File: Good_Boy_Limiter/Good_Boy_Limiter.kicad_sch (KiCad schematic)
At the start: 28 parts, among them Q2 AO3422, SW3 RESET1, SW4 BOOT1, U1 ESP32-S3-WROOM-1, U2 TC4427EOA_C636891, U3 LM2576HVR-12, U8 B3B-XH-A, U9 LM393DR2G

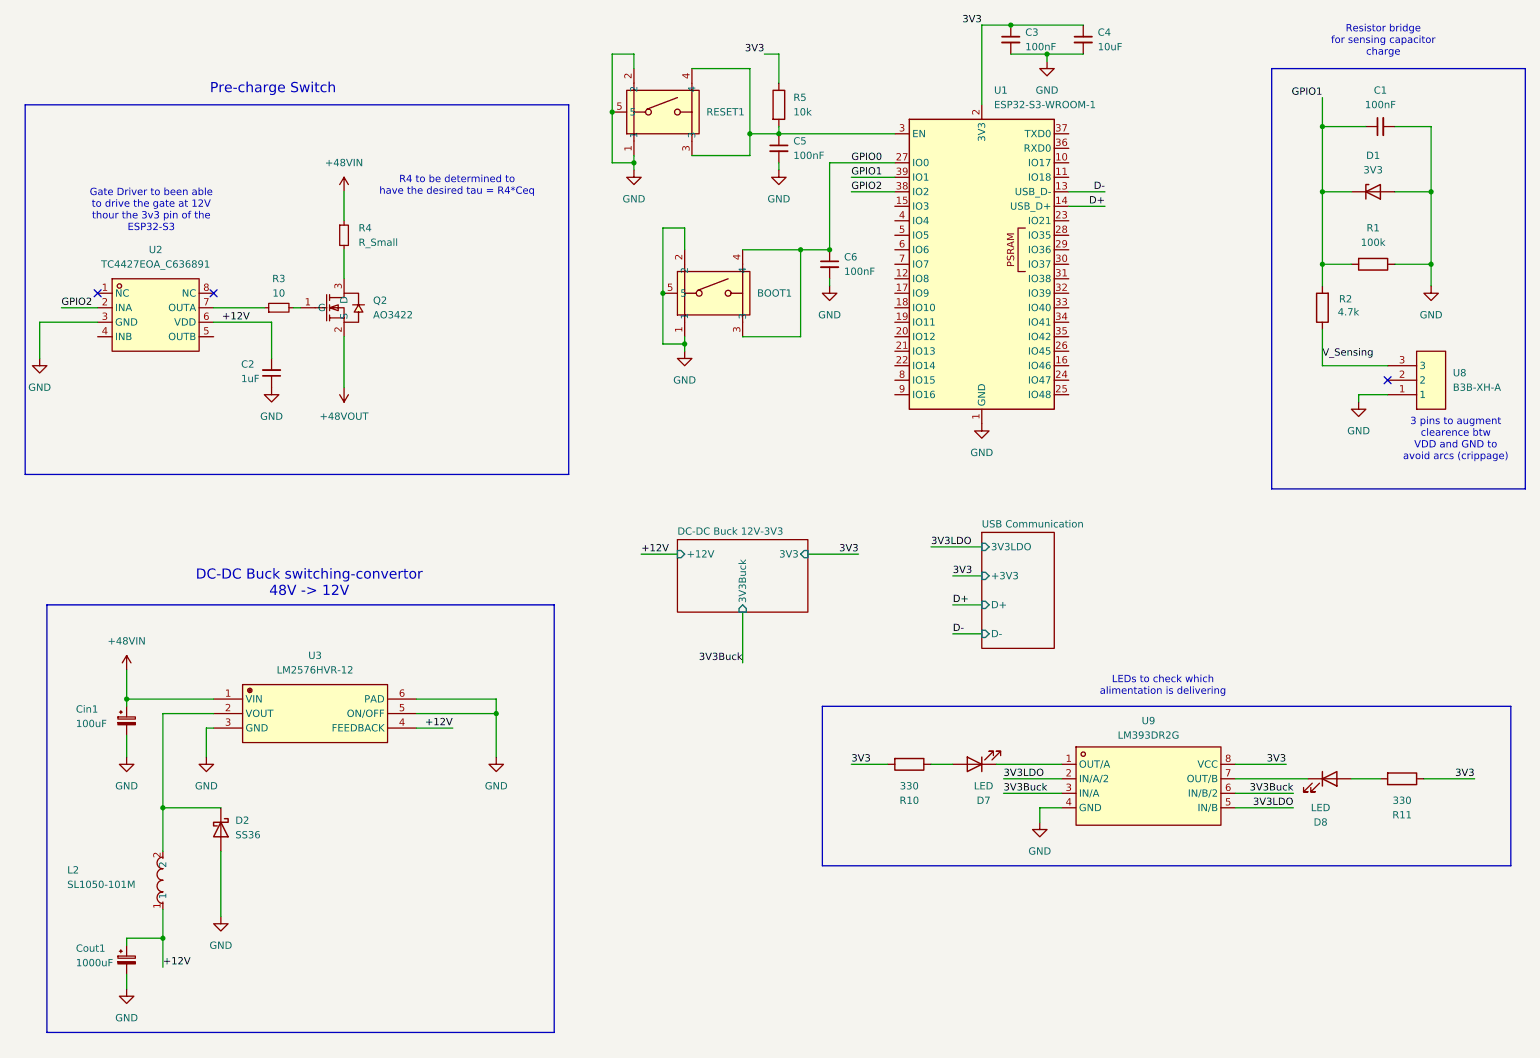
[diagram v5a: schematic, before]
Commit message: Added all footprints
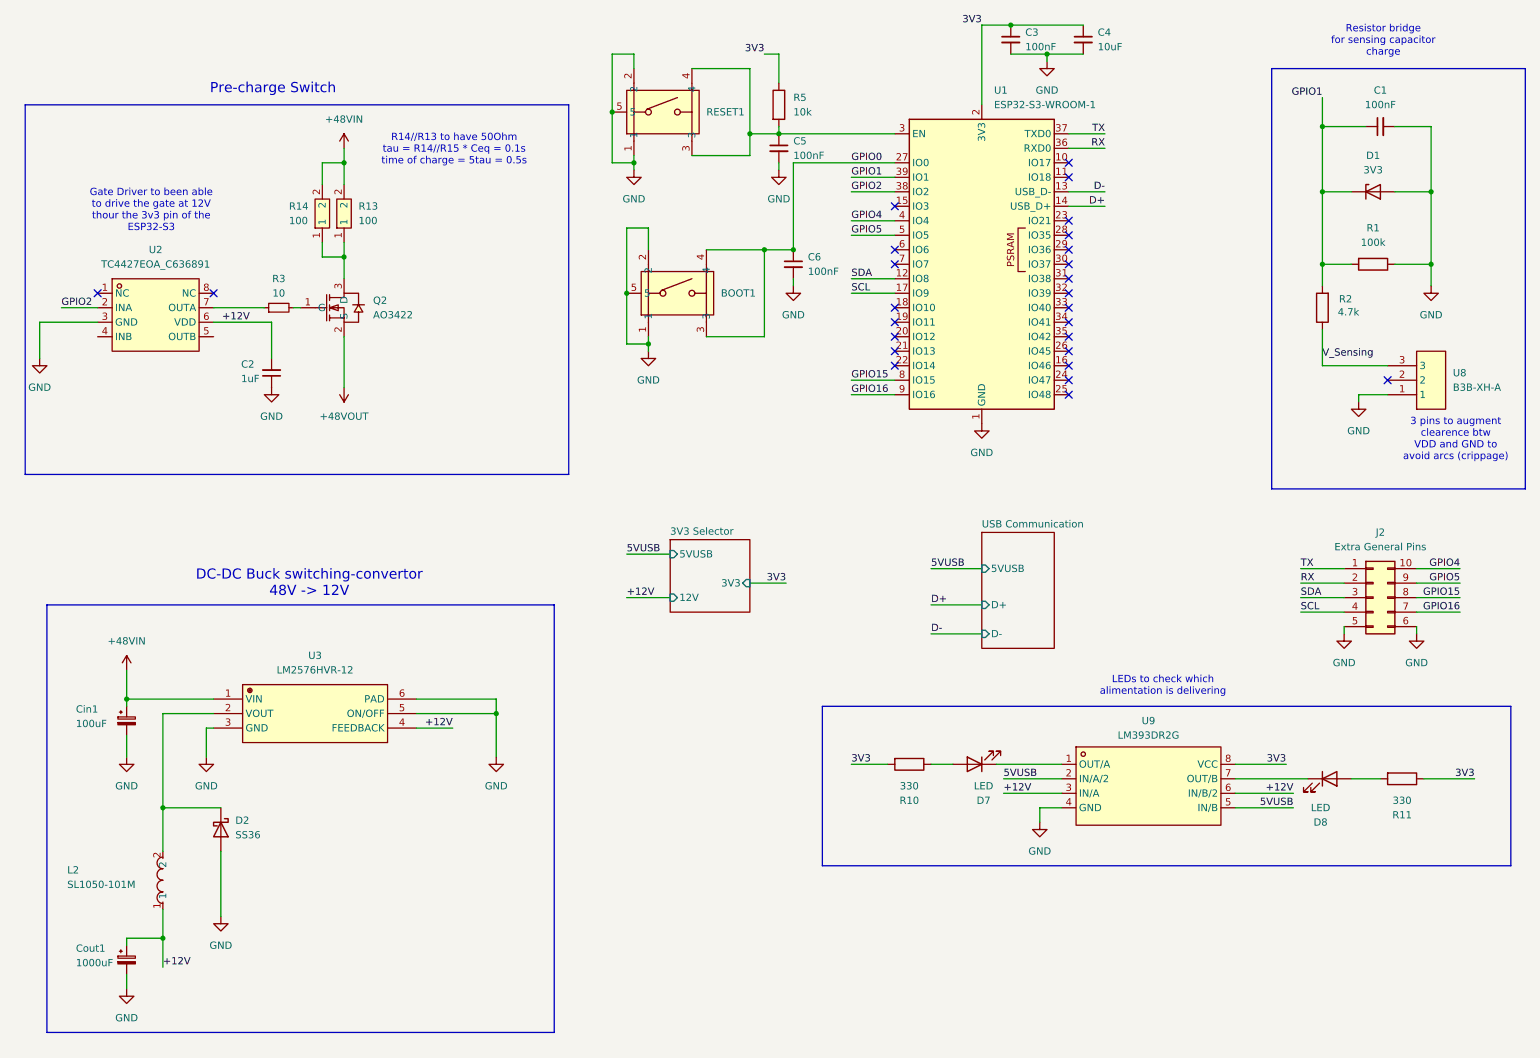
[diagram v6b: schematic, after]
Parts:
- removed R4: R_Small, symbol Device:R_Small
- added J2: Extra General Pins, Connector_PinHeader_2.54mm:PinHeader_2x05_P2.54mm_Vertical, symbol Connector_Generic:Conn_02x05_Counter_Clockwise
- added R13, R14: 100, easyeda2kicad:RES-SMD_L6.7-W4.0-LS7.9, symbol easyeda2kicad:SMW2100RJT
- C1: footprint Capacitor_SMD:C_0201_0603Metric -> Capacitor_SMD:C_0201_0603Metric_Pad0.64x0.40mm_HandSolder; LCSC Part (none) -> C1590
- C2: footprint (none) -> Capacitor_SMD:C_0805_2012Metric_Pad1.18x1.45mm_HandSolder; LCSC Part (none) -> C53084463
- C3, C5: footprint (none) -> Capacitor_SMD:C_0201_0603Metric_Pad0.64x0.40mm_HandSolder; LCSC Part (none) -> C1590
- C4: footprint (none) -> Capacitor_SMD:C_0201_0603Metric_Pad0.64x0.40mm_HandSolder; LCSC Part (none) -> C1691
- C6: footprint (none) -> Capacitor_SMD:C_0402_1005Metric_Pad0.74x0.62mm_HandSolder; LCSC Part (none) -> C1525
- R1, R2: footprint Resistor_SMD:R_0201_0603Metric -> Resistor_SMD:R_0603_1608Metric_Pad0.98x0.95mm_HandSolder
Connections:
- net 3V3Buck is gone; now on net +12V: U9.3 (IN/A), U9.6 (IN/B/2)
- net +48VIN: now also R13.2, R14.2
- net GND: now also J2.5 (Pin_5), J2.6 (Pin_6)
- net SDA: now reaches U1.12 (IO8)
- net SDA: now also J2.3 (Pin_3)
- net SCL: now reaches U1.17 (IO9)
- net SCL: now also J2.4 (Pin_4)
- net RX: now reaches U1.36 (RXD0)
- net RX: now also J2.2 (Pin_2)
- net TX: now reaches U1.37 (TXD0)
- net TX: now also J2.1 (Pin_1)
- net GPIO4: now reaches U1.4 (IO4)
- net GPIO4: now also J2.10 (Pin_10)
- net GPIO5: now reaches U1.5 (IO5)
- net GPIO5: now also J2.9 (Pin_9)
- net GPIO15: now reaches U1.8 (IO15)
- net GPIO15: now also J2.8 (Pin_8)
- net GPIO16: now reaches U1.9 (IO16)
- net GPIO16: now also J2.7 (Pin_7)
- net at Q2.3 (D): now also R13.1, R14.1
- net 3V3LDO renamed 5VUSB
- no-connect marks 3 -> 26
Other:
- removed sheet DC-DC Buck 12V-3V3
- added sheet 3V3 Selector (3V3_selector.kicad_sch)
- sheet USB Communication ports: added 5VUSB; removed +3V3, 3V3LDO
- note added: "R14//R13 to have 50Ohm tau = R14//R15 * Ceq = 0.1s time of charge = 5tau = 0.5s"
- note removed: "R4 to be determined to have the desired tau = R4*Ceq"
- moved on the sheet: C6

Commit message: Added mounting holes and test points
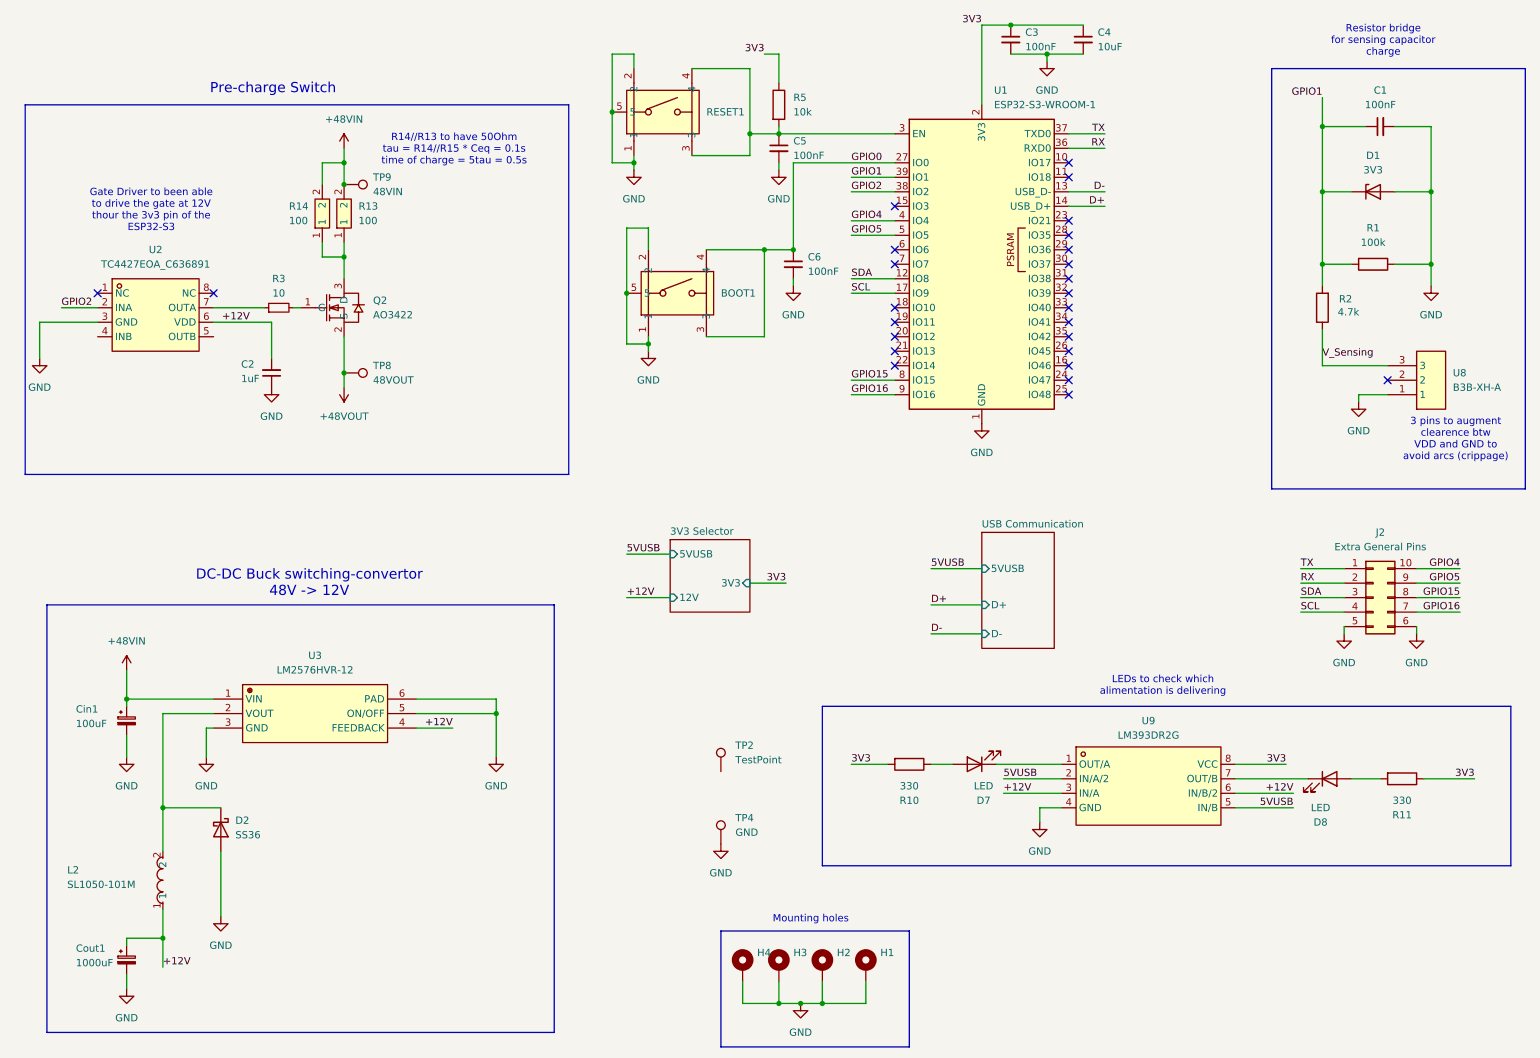
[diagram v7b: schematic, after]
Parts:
- added H1, H2, H3, H4: MountingHole_Pad, MountingHole:MountingHole_3.2mm_M3_DIN965_Pad, symbol Mechanical:MountingHole_Pad
- added TP2: TestPoint, symbol Connector:TestPoint
- added TP4: GND, symbol Connector:TestPoint
- added TP8: 48VOUT, TestPoint:TestPoint_Pad_D2.0mm, symbol Connector:TestPoint
- added TP9: 48VIN, TestPoint:TestPoint_Pad_D2.0mm, symbol Connector:TestPoint
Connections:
- net +48VIN: now also TP9.1
- net +48VOUT: now also TP8.1
- net GND: now also H1.1, H2.1, H3.1, H4.1, TP4.1
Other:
- note added: "Mounting holes"

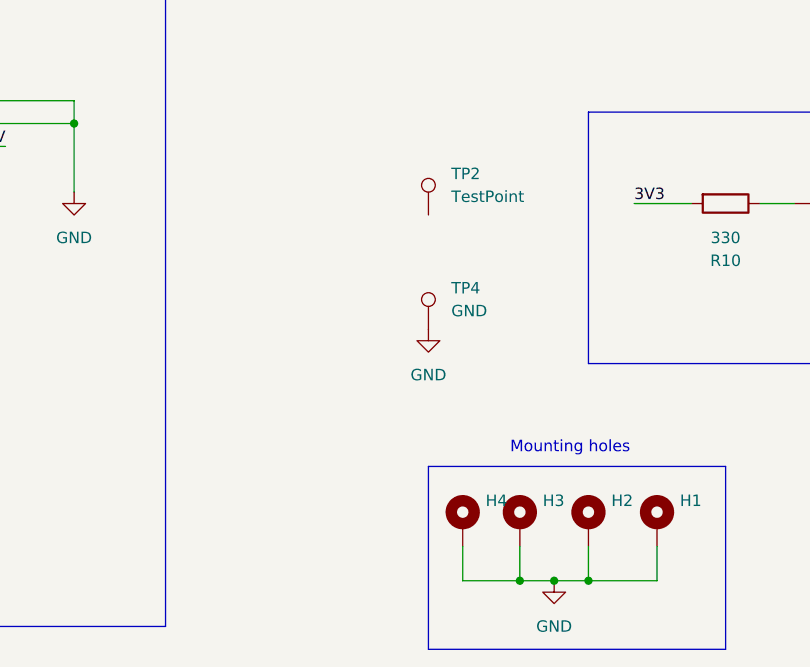
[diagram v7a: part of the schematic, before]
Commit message: started some routing
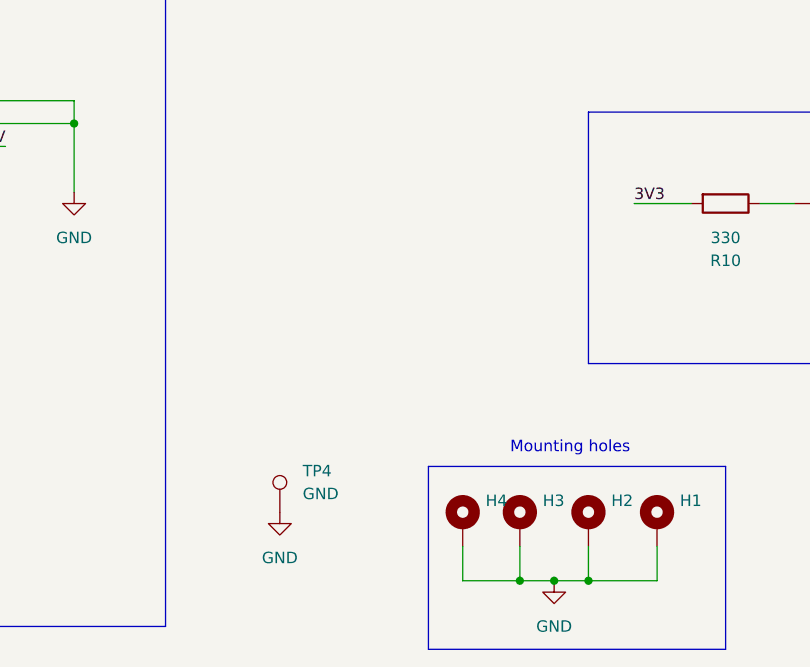
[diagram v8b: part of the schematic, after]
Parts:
- removed TP2: TestPoint, symbol Connector:TestPoint
- TP4: footprint (none) -> TestPoint:TestPoint_Pad_D2.0mm
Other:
- moved on the sheet: TP4
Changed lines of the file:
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@@
 	(symbol
 		(lib_id "Connector:TestPoint")
-		(at 139.7 161.29 0)
+		(at 123.19 181.61 0)
 		(unit 1)
 		(exclude_from_sim no)
@@
 		(fields_autoplaced yes)
 		(property "Reference" "TP4"
-			(at 142.24 156.7179 0)
+			(at 125.73 177.0379 0)
 			(effects
 				(font
@@
 		)
 		(property "Value" "GND"
-			(at 142.24 159.2579 0)
+			(at 125.73 179.5779 0)
 			(effects
 				(font
@@
 			)
 		)
-		(property "Footprint" ""
-			(at 144.78 161.29 0)
+		(property "Footprint" "TestPoint:TestPoint_Pad_D2.0mm"
+			(at 128.27 181.61 0)
 			(effects
 				(font
@@
 		)
 		(property "Datasheet" "~"
-			(at 144.78 161.29 0)
+			(at 128.27 181.61 0)
 			(effects
 				(font
@@
 		)
 		(property "Description" "test point"
-			(at 139.7 161.29 0)
+			(at 123.19 181.61 0)
 			(effects
 				(font
@@
 	(symbol
 		(lib_id "power:GND")
-		(at 139.7 161.29 0)
+		(at 123.19 181.61 0)
 		(unit 1)
 		(exclude_from_sim no)
@@
 		(fields_autoplaced yes)
 		(property "Reference" "#PWR040"
-			(at 139.7 167.64 0)
+			(at 123.19 187.96 0)
 			(effects
 				(font
@@
 		)
 		(property "Value" "GND"
-			(at 139.7 166.37 0)
+			(at 123.19 186.69 0)
 			(effects
 				(font
@@
 		)
 		(property "Footprint" ""
-			(at 139.7 161.29 0)
+			(at 123.19 181.61 0)
 			(effects
 				(font
@@
 		)
 		(property "Datasheet" ""
-			(at 139.7 161.29 0)
+			(at 123.19 181.61 0)
 			(effects
 				(font
@@
 		)
 		(property "Description" "Power symbol creates a global label with name \"GND\" , ground"
-			(at 139.7 161.29 0)
+			(at 123.19 181.61 0)
 			(effects
 				(font
@@
 					(unit 1)
 				)
-			)
-		)
-	)
-	(symbol
-		(lib_id "Connector:TestPoint")
-		(at 139.7 148.59 0)
-		(unit 1)
-		(exclude_from_sim no)
-		(in_bom yes)
-		(on_board yes)
-		(dnp no)
-		(fields_autoplaced yes)
-		(property "Reference" "TP2"
-			(at 142.24 144.0179 0)
-			(effects
-				(font
-					(size 1.27 1.27)
-				)
-				(justify left)
-			)
-		)
-		(property "Value" "TestPoint"
-			(at 142.24 146.5579 0)
-			(effects
-				(font
-					(size 1.27 1.27)
-				)
-				(justify left)
-			)
-		)
-		(property "Footprint" ""
-			(at 144.78 148.59 0)
-			(effects
-				(font
-					(size 1.27 1.27)
-				)
-				(hide yes)
-			)
-		)
-		(property "Datasheet" "~"
-			(at 144.78 148.59 0)
-			(effects
-				(font
-					(size 1.27 1.27)
-				)
-				(hide yes)
-			)
-		)
-		(property "Description" "test point"
-			(at 139.7 148.59 0)
-			(effects
-				(font
-					(size 1.27 1.27)
-				)
-				(hide yes)
-			)
-		)
-		(pin "1"
-		)
-		(instances
-			(project ""
-				(path "/e6249df1-5b78-4b75-b804-4c6c30b1afc2"
-					(reference "TP2")
-					(unit 1)
-				)
